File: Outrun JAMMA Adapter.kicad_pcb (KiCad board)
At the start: 2 copper layers, 111 x 77.8 mm, 31 parts, among them U1 LM386, U2 MCP4902, U3 328P

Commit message: minor cleanup, populated image
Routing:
- net +5V: track 360.9 -> 348.8 mm
- net PB1: track 77.3 -> 75.0 mm
- net GND: track 608.3 -> 606.5 mm
- net SPKR+: track 70.0 -> 71.1 mm
- net AUDIO_L: track 55.6 -> 56.3 mm
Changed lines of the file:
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@@
 	)
 	(gr_rect
-		(start 194.067071 77.226703)
-		(end 203.958807 81.458316)
+		(start 97.390799 78.427694)
+		(end 107.282535 82.659307)
 		(stroke
 			(width 0.1)
@@
 	)
 	(gr_text "PARTS SIDE"
-		(at 195.476272 79.799009 0)
+		(at 98.8 81 0)
 		(layer "F.SilkS")
 		(effects
@@
 	)
 	(segment
+		(start 172.87875 82.2)
+		(end 167.3 76.62125)
+		(width 0.5)
+		(layer "B.Cu")
+		(net "GND")
+	)
+	(segment
 		(start 95.8 100)
 		(end 95.8 98.2)
@@
 	)
 	(segment
-		(start 167.3 73.1425)
-		(end 170.77875 76.62125)
-		(width 0.5)
-		(layer "B.Cu")
-		(net "GND")
-	)
-	(segment
 		(start 98.4 87.79)
 		(end 96.01 87.79)
@@
 	)
 	(segment
+		(start 167.3 69.2425)
+		(end 167.3 76.62125)
+		(width 0.5)
+		(layer "B.Cu")
+		(net "GND")
+	)
+	(segment
 		(start 153.02125 76.62125)
 		(end 152.12 75.72)
@@
 	)
 	(segment
-		(start 167.3 69.2425)
-		(end 167.3 73.1425)
-		(width 0.5)
-		(layer "B.Cu")
-		(net "GND")
-	)
-	(segment
 		(start 157.323476 122.421752)
 		(end 152.4 122.421752)
@@
 	)
 	(segment
-		(start 170.77875 76.62125)
-		(end 153.02125 76.62125)
-		(width 0.5)
-		(layer "B.Cu")
-		(net "GND")
-	)
-	(segment
 		(start 115.58 100)
 		(end 95.8 100)
@@
 	)
 	(segment
-		(start 170.77875 76.62125)
-		(end 175.75 81.5925)
-		(width 0.5)
-		(layer "B.Cu")
-		(net "GND")
-	)
-	(segment
 		(start 152.264851 122.286603)
 		(end 152.4 122.421752)
@@
 	)
 	(segment
-		(start 175.75 81.5925)
+		(start 175.75 82.2)
+		(end 172.87875 82.2)
+		(width 0.5)
+		(layer "B.Cu")
+		(net "GND")
+	)
+	(segment
+		(start 175.75 82.2)
 		(end 175.75 83.6)
 		(width 0.5)
@@
 	)
 	(segment
+		(start 153.02125 76.62125)
+		(end 167.3 76.62125)
+		(width 0.5)
+		(layer "B.Cu")
+		(net "GND")
+	)
+	(segment
 		(start 110.322146 101.2)
 		(end 103.769296 101.2)
@@
 	)
 	(segment
-		(start 130 107.120704)
-		(end 138.560352 98.560352)
-		(width 0.2)
-		(layer "F.Cu")
-		(net "+5V")
-	)
-	(segment
 		(start 140.594851 107.825555)
 		(end 140.594851 107.865555)
@@
 	)
 	(segment
-		(start 167.3 69.2425)
-		(end 167.3 72.3)
+		(start 178.4 93)
+		(end 178.4 99.6)
 		(width 0.5)
 		(layer "F.Cu")
@@
 	)
 	(segment
-		(start 178.4 93)
-		(end 178.4 99.6)
+		(start 167.3 74.3)
+		(end 174.5 81.5)
+		(width 0.5)
+		(layer "F.Cu")
+		(net "SPKR+")
+	)
+	(segment
+		(start 167.3 69.2425)
+		(end 167.3 74.3)
 		(width 0.5)
 		(layer "F.Cu")
@@
 	)
 	(segment
-		(start 167.3 72.3)
+		(start 174.5 81.5)
 		(end 176.5 81.5)
 		(width 0.5)
@@
 	)
 	(segment
-		(start 145.42 87.78)
-		(end 146.974695 86.225305)
+		(start 148.2 88.4)
+		(end 148.6 88)
 		(width 0.2)
 		(layer "F.Cu")
@@
 	)
 	(segment
-		(start 192.05962 111.25962)
-		(end 187.94038 111.25962)
+		(start 154.63 90.56137)
+		(end 154.63 89.464314)
 		(width 0.2)
 		(layer "F.Cu")
@@
 	)
 	(segment
-		(start 156.668629 92.6)
-		(end 154.63 90.56137)
+		(start 192.05962 111.25962)
+		(end 187.94038 111.25962)
 		(width 0.2)
 		(layer "F.Cu")
@@
 	)
 	(segment
-		(start 169.399998 92.6)
-		(end 156.668629 92.6)
+		(start 136.04 88.4)
+		(end 148.2 88.4)
 		(width 0.2)
 		(layer "F.Cu")
@@
 	(segment
 		(start 135.42 87.78)
-		(end 145.42 87.78)
+		(end 136.04 88.4)
 		(width 0.2)
 		(layer "F.Cu")
@@
 	)
 	(segment
-		(start 185.74038 109.05962)
-		(end 185.74038 108.94038)
+		(start 185.74038 108.94038)
+		(end 169.399998 92.6)
 		(width 0.2)
 		(layer "F.Cu")
@@
 	)
 	(segment
-		(start 154.63 90.56137)
-		(end 154.63 89.464314)
+		(start 154.63 89.464314)
+		(end 152.182843 87.017157)
 		(width 0.2)
 		(layer "F.Cu")
@@
 	)
 	(segment
-		(start 154.63 89.464314)
-		(end 149.35962 84.193934)
+		(start 185.74038 109.05962)
+		(end 185.74038 108.94038)
 		(width 0.2)
 		(layer "F.Cu")
@@
 	)
 	(segment
-		(start 196.8 116)
-		(end 192.05962 111.25962)
+		(start 156.668629 92.6)
+		(end 154.63 90.56137)
 		(width 0.2)
 		(layer "F.Cu")
@@
 	)
 	(segment
-		(start 185.74038 108.94038)
-		(end 169.399998 92.6)
+		(start 196.8 116)
+		(end 192.05962 111.25962)
 		(width 0.2)
 		(layer "F.Cu")
@@
 	)
 	(segment
-		(start 149.35962 84.193934)
-		(end 149.35962 83.84038)
+		(start 169.399998 92.6)
+		(end 156.668629 92.6)
 		(width 0.2)
 		(layer "F.Cu")
@@
 	)
 	(via
-		(at 146.974695 86.225305)
+		(at 148.6 88)
 		(size 0.6)
 		(drill 0.3)
@@
 	)
 	(via
-		(at 149.35962 83.84038)
+		(at 152.182843 87.017157)
 		(size 0.6)
 		(drill 0.3)
@@
 	)
 	(segment
-		(start 146.974695 86.225305)
-		(end 149.35962 83.84038)
+		(start 185.85962 109.05962)
+		(end 187.94038 111.14038)
 		(width 0.2)
 		(layer "B.Cu")
@@
 	)
 	(segment
-		(start 185.85962 109.05962)
-		(end 187.94038 111.14038)
+		(start 148.6 88)
+		(end 149.582843 87.017157)
+		(width 0.2)
+		(layer "B.Cu")
+		(net "PB1")
+	)
+	(segment
+		(start 149.582843 87.017157)
+		(end 152.182843 87.017157)
 		(width 0.2)
 		(layer "B.Cu")
@@
 	)
 	(segment
-		(start 164.08 85)
-		(end 149.95648 85)
+		(start 121.611033 114.775555)
+		(end 121.611033 113.223281)
+		(width 0.2)
+		(layer "B.Cu")
+		(net "AUDIO_L")
+	)
+	(segment
+		(start 121.611033 113.223281)
+		(end 130.834314 104)
+		(width 0.2)
+		(layer "B.Cu")
+		(net "AUDIO_L")
+	)
+	(segment
+		(start 130.834314 104)
+		(end 131.6 104)
+		(width 0.2)
+		(layer "B.Cu")
+		(net "AUDIO_L")
+	)
+	(segment
+		(start 148.4 97.4)
+		(end 157.8 88)
 		(width 0.2)
 		(layer "B.Cu")
@@
 	)
 	(segment
-		(start 121.611033 113.345448)
-		(end 121.611033 114.775555)
+		(start 138.2 97.4)
+		(end 148.4 97.4)
 		(width 0.2)
 		(layer "B.Cu")
@@
 	)
 	(segment
-		(start 149.95648 85)
-		(end 121.611033 113.345448)
+		(start 164.08 85.92)
+		(end 164.08 85)
 		(width 0.2)
 		(layer "B.Cu")
@@
 	)
 	(segment
-		(start 124.2777 111.5223)
-		(end 124.2777 114.775555)
+		(start 162 88)
+		(end 164.08 85.92)
+		(width 0.2)
+		(layer "B.Cu")
+		(net "AUDIO_L")
+	)
+	(segment
+		(start 131.6 104)
+		(end 138.2 97.4)
+		(width 0.2)
+		(layer "B.Cu")
+		(net "AUDIO_L")
+	)
+	(segment
+		(start 157.8 88)
+		(end 162 88)
+		(width 0.2)
+		(layer "B.Cu")
+		(net "AUDIO_L")
+	)
+	(segment
+		(start 124.2777 114.775555)
+		(end 124.2777 111.887986)
 		(width 0.2)
 		(layer "B.Cu")
@@
 	)
 	(segment
-		(start 129.294982 106.470704)
-		(end 129.294982 106.505018)
+		(start 157.965686 88.4)
+		(end 165.76 88.4)
 		(width 0.2)
 		(layer "B.Cu")
@@
 	)
 	(segment
-		(start 129.294982 106.505018)
-		(end 124.2777 111.5223)
+		(start 124.2777 111.887986)
+		(end 138.365686 97.8)
 		(width 0.2)
 		(layer "B.Cu")
@@
 	)
 	(segment
-		(start 149.615686 86.15)
-		(end 129.294982 106.470704)
+		(start 165.76 88.4)
+		(end 169.16 85)
 		(width 0.2)
 		(layer "B.Cu")
@@
 	)
 	(segment
-		(start 168.01 86.15)
-		(end 149.615686 86.15)
+		(start 138.365686 97.8)
+		(end 148.565686 97.8)
 		(width 0.2)
 		(layer "B.Cu")
@@
 	)
 	(segment
-		(start 169.16 85)
-		(end 168.01 86.15)
+		(start 148.565686 97.8)
+		(end 157.965686 88.4)
 		(width 0.2)
 		(layer "B.Cu")
@@
 		(net "C5_R4")
 	)
-	(group ""
-		(members "eef51e2e-4a43-4663-8162-23505cc657ca" "fc084109-c243-4ba2-be16-cb9fba5ce99c")
-	)
 	(embedded_fonts no)

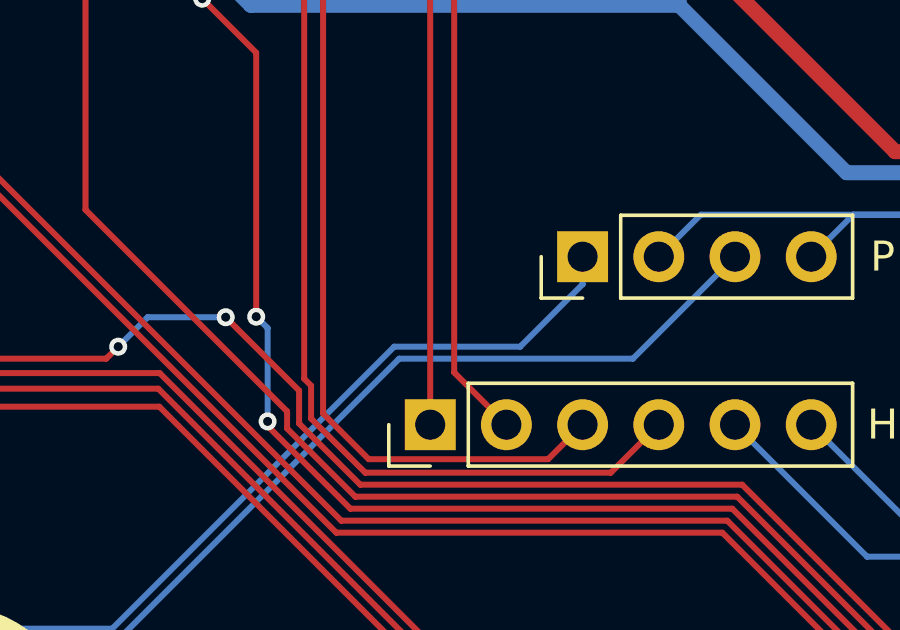
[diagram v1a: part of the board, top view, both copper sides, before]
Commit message: add pin 1 labels
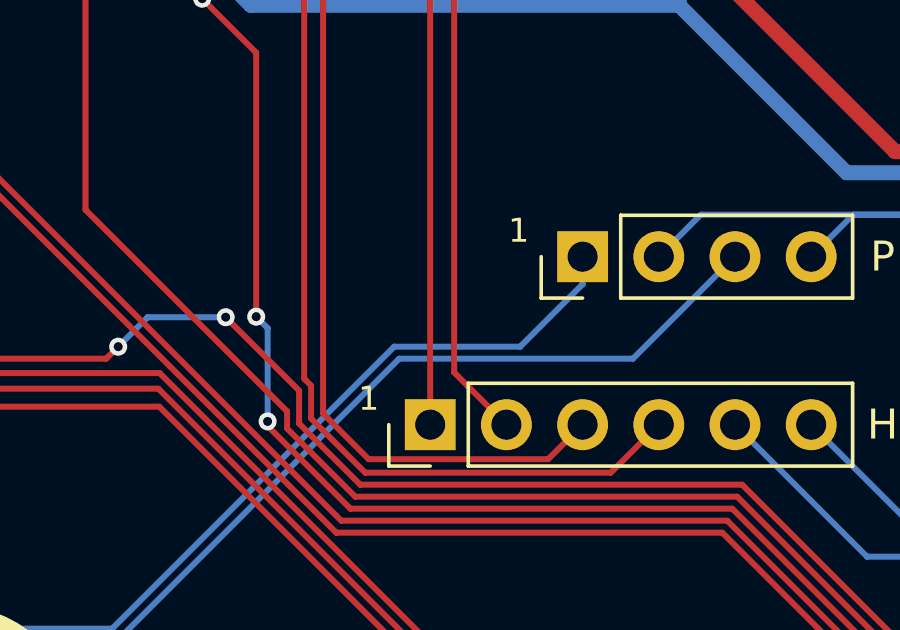
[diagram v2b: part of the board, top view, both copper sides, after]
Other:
- board text added: "1"
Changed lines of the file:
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@@
+		)
+	)
+	(gr_text "1"
+		(at 156.6 90.2 0)
+		(layer "F.SilkS")
+		(effects
+			(font
+				(size 0.8 0.8)
+				(thickness 0.1)
+			)
+			(justify left bottom)
+		)
+	)
+	(gr_text "1"
+		(at 161.6 84.6 0)
+		(layer "F.SilkS")
+		(effects
+			(font
+				(size 0.8 0.8)
+				(thickness 0.1)
+			)
+			(justify left bottom)
 		)
 	)

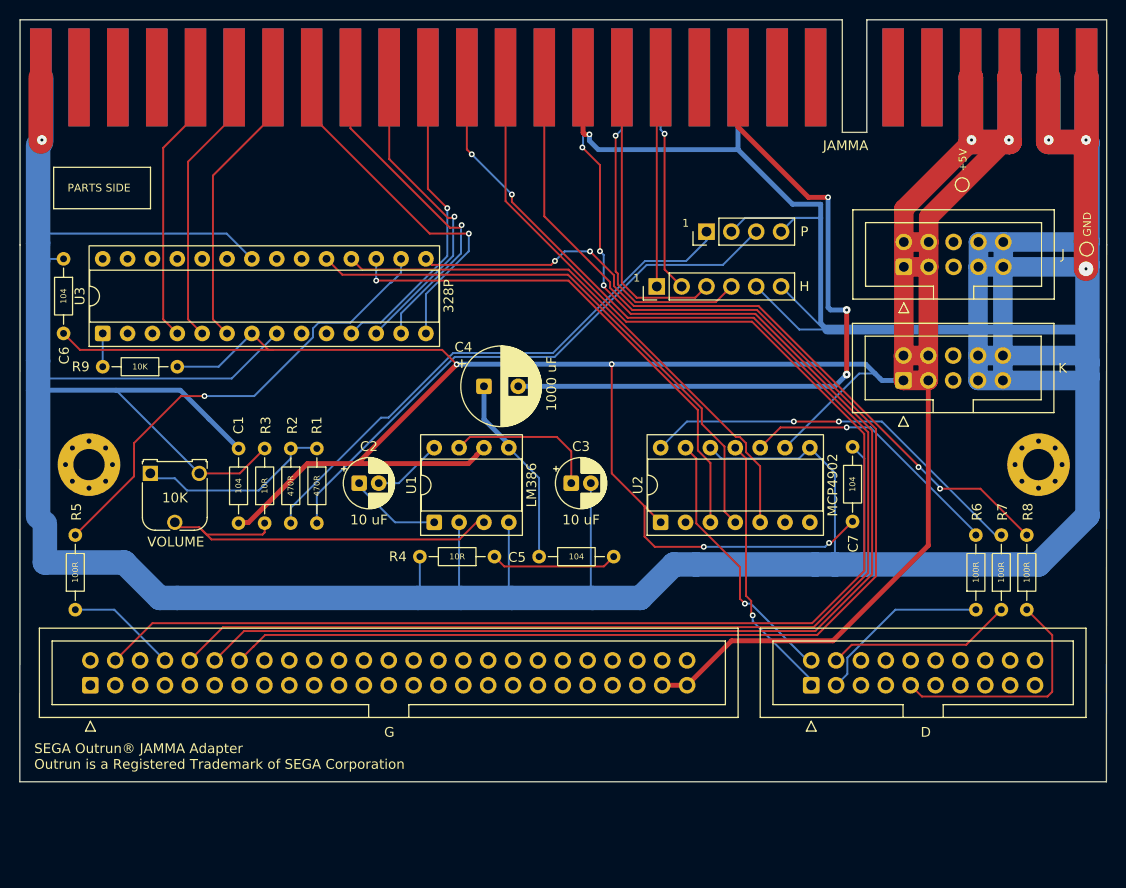
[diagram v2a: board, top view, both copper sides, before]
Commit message: add relief for size of AMP connectors
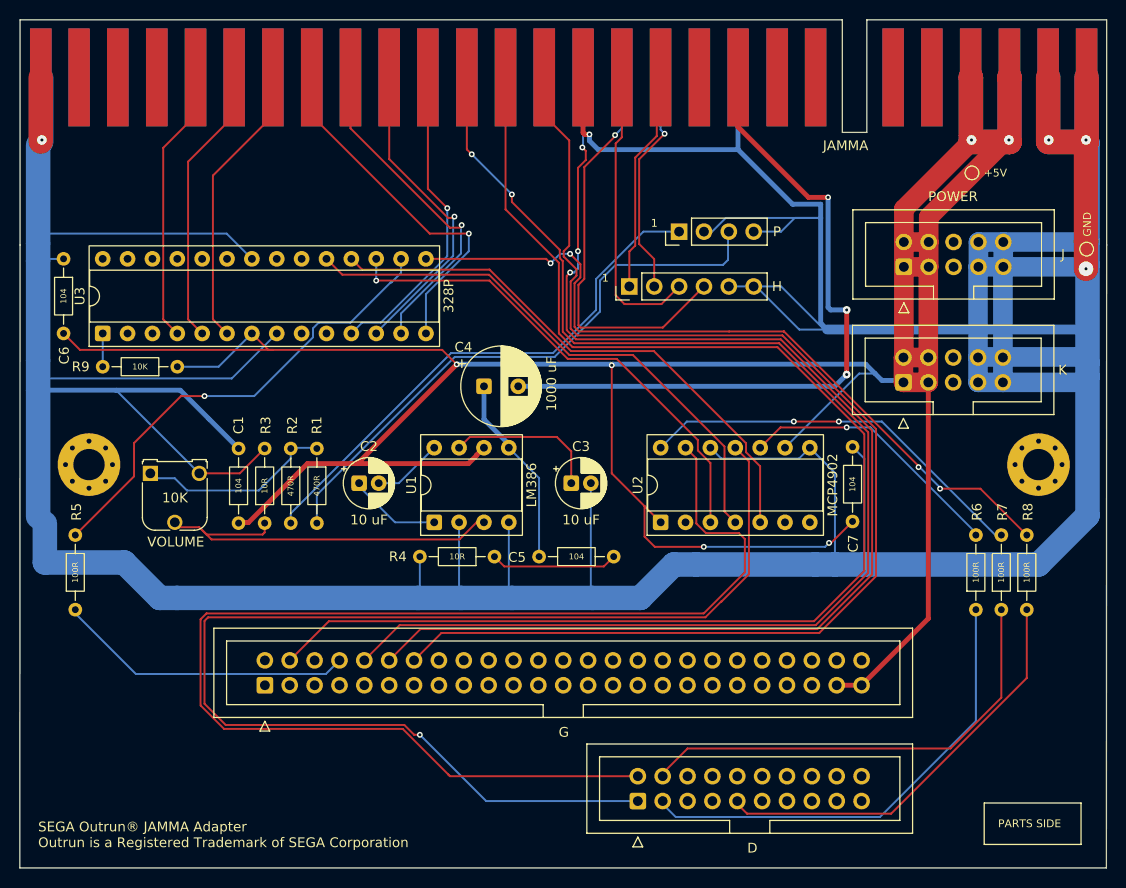
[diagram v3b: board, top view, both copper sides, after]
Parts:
- moved D 21.3 mm to (157.1, 143.2)
- moved G 17.8 mm to (119.0, 131.3)
- moved H 2.80 mm to (156.2, 90.6)
- moved P 2.80 mm to (161.3, 85.0)
- moved +5V 1.56 mm to (191.2, 79.0), turned to -90 degrees
- moved K 0.20 mm to (184.2, 100.4)
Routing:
- net REFA: track 27.6 -> 131.5 mm, vias 1 -> 0
- net REFB: track 27.5 -> 127.9 mm
- net STEER: track 18.5 -> 48.4 mm
- net ACCEL: track 19.0 -> 47.2 mm
- net SHIFT: track 11.3 -> 30.5 mm
- net BRK: track 24.6 -> 43.1 mm
- net COIN_1: track 153.4 -> 140.3 mm
- net 1P_START: track 148.1 -> 135.0 mm
- net +5V: track 348.8 -> 335.8 mm
- net GND: track 606.5 -> 618.6 mm
- net TEST: track 141.0 -> 129.0 mm
- net SERVICE: track 141.3 -> 130.1 mm
- net VID_CSYNC: track 34.5 -> 41.8 mm
- net PB1: track 75.0 -> 78.6 mm
- net AUDIO_L: track 56.3 -> 54.4 mm
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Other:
- board size 111 x 77.8 mm -> 111 x 86.6 mm
- board text added: "POWER"

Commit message: remap pins for ribbon cable, change audio/video to larger connector
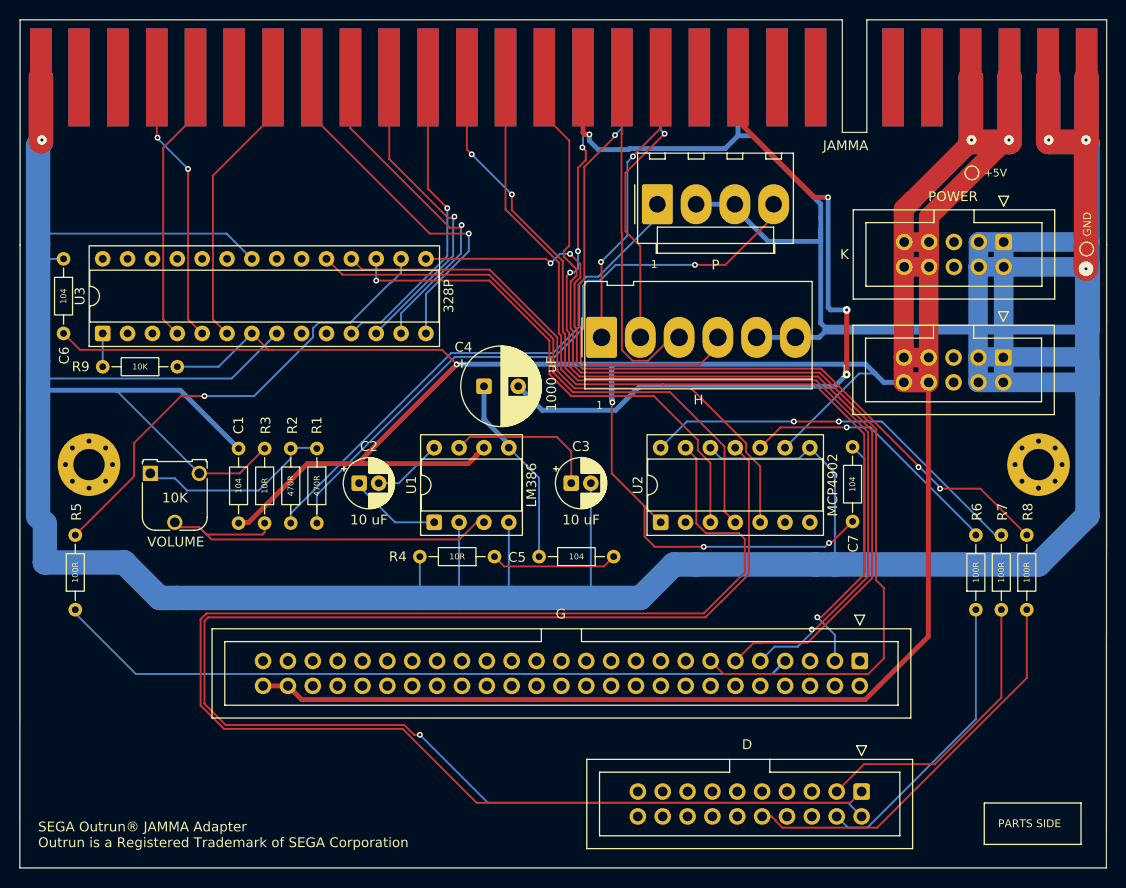
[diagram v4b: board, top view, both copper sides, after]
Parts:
- H: footprint Connector_PinHeader_2.54mm:PinHeader_1x06_P2.54mm_Vertical -> Connector_Molex:Molex_KK-396_5273-06A_1x06_P3.96mm_Vertical
- P: footprint Connector_PinHeader_2.54mm:PinHeader_1x04_P2.54mm_Vertical -> Connector_Molex:Molex_KK-396_A-41791-0004_1x04_P3.96mm_Vertical
- moved G 60.8 mm to (179.7, 128.9), turned to -90 degrees
- moved D 22.9 mm to (179.9, 142.2), turned to -90 degrees
- moved K 17.6 mm to (194.4, 86.1), turned to -90 degrees
- moved J 13.7 mm to (194.4, 97.9), turned to -90 degrees
- moved H 5.92 mm to (153.4, 95.8), turned to 0 degrees
- moved P 3.57 mm to (159.1, 82.2), turned to 0 degrees
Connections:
- D pad 1: REFB -> REFA
- D pad 10: (no net) -> BRK
- D pad 2: REFA -> REFB
- D pad 3: STEER -> ACCEL
- D pad 4: ACCEL -> STEER
- D pad 9: BRK -> (no net)
- G pad 10: 1P_START -> (no net)
- G pad 11: (no net) -> SERVICE
- G pad 12: SERVICE -> (no net)
- G pad 13: (no net) -> TEST
- G pad 14: TEST -> (no net)
- G pad 3: (no net) -> COIN_1
- G pad 4: COIN_1 -> (no net)
- G pad 47: +5V -> (no net)
- G pad 48: (no net) -> +5V
- G pad 49: +5V -> (no net)
- G pad 50: (no net) -> +5V
- G pad 7: (no net) -> SHIFT
- G pad 8: SHIFT -> (no net)
- G pad 9: (no net) -> 1P_START
- J pad 1: +5V -> GND
- J pad 10: GND -> +5V
- J pad 2: +5V -> GND
- J pad 3: +5V -> GND
- J pad 4: +5V -> GND
- J pad 7: GND -> +5V
- J pad 8: GND -> +5V
- J pad 9: GND -> +5V
- K pad 1: +5V -> GND
- K pad 10: GND -> +5V
- K pad 2: +5V -> GND
- K pad 3: +5V -> GND
- K pad 4: +5V -> GND
- K pad 7: GND -> +5V
- K pad 8: GND -> +5V
- K pad 9: GND -> +5V
- P pad 3: AUDIO_R -> GND
- P pad 4: GND -> AUDIO_R
- U3 pad 5: 1P_B2 -> 1P_B4
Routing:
- net +5V: track 335.8 -> 429.0 mm
- net COIN_1: track 140.3 -> 92.0 mm, vias 0 -> 1
- net SHIFT: track 30.5 -> 77.7 mm
- net 1P_START: track 135.0 -> 97.0 mm, vias 2 -> 3
- net SERVICE: track 130.1 -> 97.6 mm
- net 1P_B2: track 28.7 -> 0.00 mm
- net 1P_B4: track 0.00 -> 28.1 mm, vias 0 -> 2
- net REFA: track 131.5 -> 156.0 mm
- net REFB: track 127.9 -> 151.4 mm
- net TEST: track 129.0 -> 107.9 mm
- net STEER: track 48.4 -> 30.5 mm
- net ACCEL: track 47.2 -> 29.8 mm
- net GND: track 618.6 -> 605.3 mm
- net VID_R: track 22.7 -> 29.1 mm, vias 0 -> 2
- net VID_G: track 23.2 -> 29.0 mm
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
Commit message: tweaks
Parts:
- moved H 1.60 mm to (153.4, 97.4)
- moved P 1.40 mm to (159.1, 83.6)
- moved R1 0.84 mm to (124.3, 108.0)
- moved R2 0.84 mm to (121.6, 108.0)
- moved C1 0.82 mm to (116.3, 115.6)
- moved R3 0.82 mm to (118.9, 115.6)
- moved C7 0.81 mm to (179.0, 107.8)
- moved R4 0.80 mm to (142.4, 119.0)
- moved C5 0.80 mm to (154.6, 119.0)
- moved C2 0.70 mm to (128.6, 111.4)
- moved C3 0.70 mm to (150.3, 111.4)
- moved U1 0.70 mm to (136.3, 115.4)
- moved U2 0.70 mm to (159.4, 115.4)
- moved VOLUME 0.70 mm to (107.3, 110.4)
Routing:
- net VID_CSYNC: track 46.8 -> 48.9 mm
- net GND: track 605.3 -> 603.3 mm
- net U3_MOSI_U2_CS: track 52.8 -> 54.8 mm
- net U3_SCK_U2_SCK: track 58.8 -> 60.8 mm
- net U3_MISO_U2_SDI: track 58.8 -> 60.8 mm
- net SPKR+: track 72.8 -> 74.8 mm
- net AUDIO_MONO: track 20.8 -> 19.1 mm
- net VID_R: track 29.1 -> 30.7 mm
- net VID_G: track 29.0 -> 30.6 mm
- net VID_B: track 35.2 -> 36.8 mm
- net U1_BYPASS: track 15.8 -> 17.2 mm
- net TEST: track 107.9 -> 109.2 mm
- net SERVICE: track 97.6 -> 98.9 mm
- net PB1: track 80.6 -> 81.9 mm
- net 1P_START: track 97.0 -> 98.3 mm
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
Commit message: update screenshots
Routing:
- net VID_B: track 36.8 -> 30.6 mm, vias 0 -> 1
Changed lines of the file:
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@@
 	)
 	(segment
-		(start 155.44 98.698721)
-		(end 156.541279 99.8)
-		(width 0.2)
-		(layer "F.Cu")
-		(net "VID_B")
-	)
-	(segment
-		(start 155.4 75.03)
-		(end 155.4 85.125686)
-		(width 0.2)
-		(layer "F.Cu")
-		(net "VID_B")
-	)
-	(segment
-		(start 155.43 75)
-		(end 155.4 75.03)
-		(width 0.2)
-		(layer "F.Cu")
-		(net "VID_B")
-	)
-	(segment
-		(start 160.498721 97.4)
-		(end 161.28 97.4)
-		(width 0.2)
-		(layer "F.Cu")
-		(net "VID_B")
-	)
-	(segment
-		(start 158.098721 99.8)
-		(end 160.498721 97.4)
-		(width 0.2)
-		(layer "F.Cu")
-		(net "VID_B")
-	)
-	(segment
-		(start 156.541279 99.8)
-		(end 158.098721 99.8)
-		(width 0.2)
-		(layer "F.Cu")
-		(net "VID_B")
-	)
-	(segment
-		(start 155.4 85.125686)
-		(end 155.44 85.165686)
-		(width 0.2)
-		(layer "F.Cu")
-		(net "VID_B")
-	)
-	(segment
-		(start 155.44 85.165686)
-		(end 155.44 98.698721)
+		(start 155.4 88)
+		(end 156.6 89.2)
 		(width 0.2)
 		(layer "F.Cu")
@@
 	(segment
 		(start 155.43 69.2425)
-		(end 155.43 75)
+		(end 155.4 69.2725)
 		(width 0.2)
 		(layer "F.Cu")
 		(net "VID_B")
 	)
+	(segment
+		(start 155.4 69.2725)
+		(end 155.4 88)
+		(width 0.2)
+		(layer "F.Cu")
+		(net "VID_B")
+	)
+	(via
+		(at 156.6 89.2)
+		(size 0.6)
+		(drill 0.3)
+		(layers "F.Cu" "B.Cu")
+		(net "VID_B")
+	)
+	(segment
+		(start 161.28 97.4)
+		(end 161.28 93.88)
+		(width 0.2)
+		(layer "B.Cu")
+		(net "VID_B")
+	)
+	(segment
+		(start 161.28 93.88)
+		(end 156.6 89.2)
+		(width 0.2)
+		(layer "B.Cu")
+		(net "VID_B")
+	)

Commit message: minor silkscreen tweaks
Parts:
- U3: value 328P -> ATMEGA328
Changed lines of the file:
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@@
 			)
 		)
-		(property "Value" "328P"
+		(property "Value" "ATMEGA328"
 			(at 3.81 35.35 90)
 			(layer "F.SilkS")
@@
 			(at 9.9 6.35 0)
 			(layer "F.Fab")
+			(hide yes)
 			(effects
 				(font
@@
 		(property "Value" "P"
 			(at 5.94 6.1 0)
-			(layer "F.Fab")
+			(layer "F.Fab" knockout)
+			(hide yes)
 			(effects
 				(font
